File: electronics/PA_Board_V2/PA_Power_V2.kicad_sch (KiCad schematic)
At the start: 35 parts, among them J5 Conn_01x02, Q1 AOD4185, U4 LMR51420, U5 MCP4725, U6 AP2204K-ADJ, U7 TLV70233, U8 INA219AxD

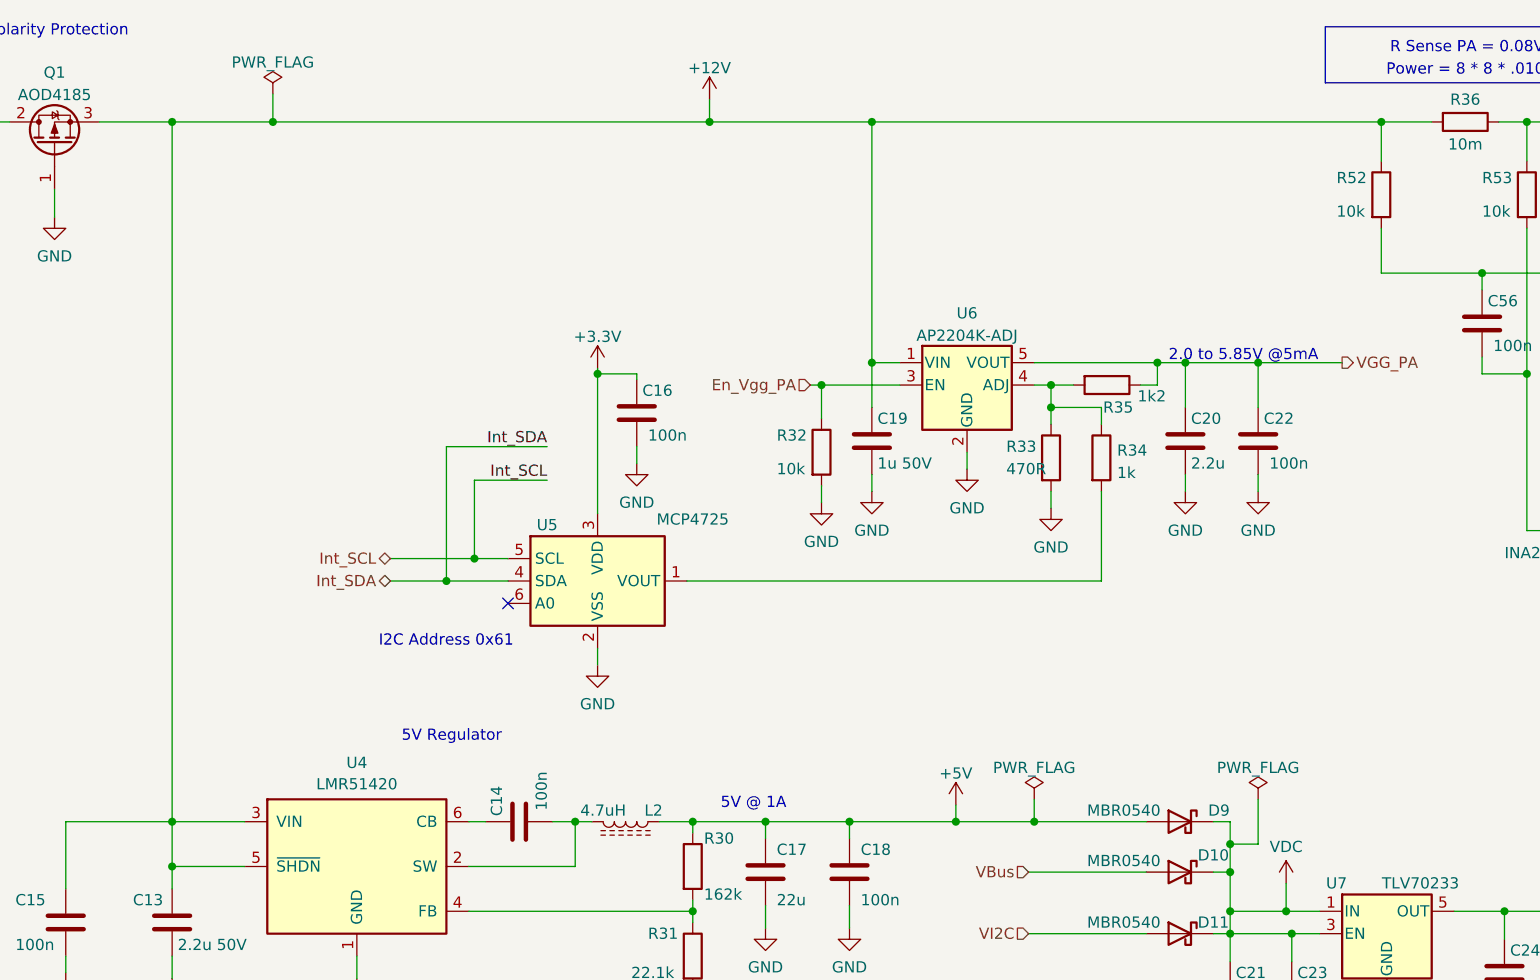
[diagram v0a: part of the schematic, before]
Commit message: Add RF Screen and some PCB and BOM changes
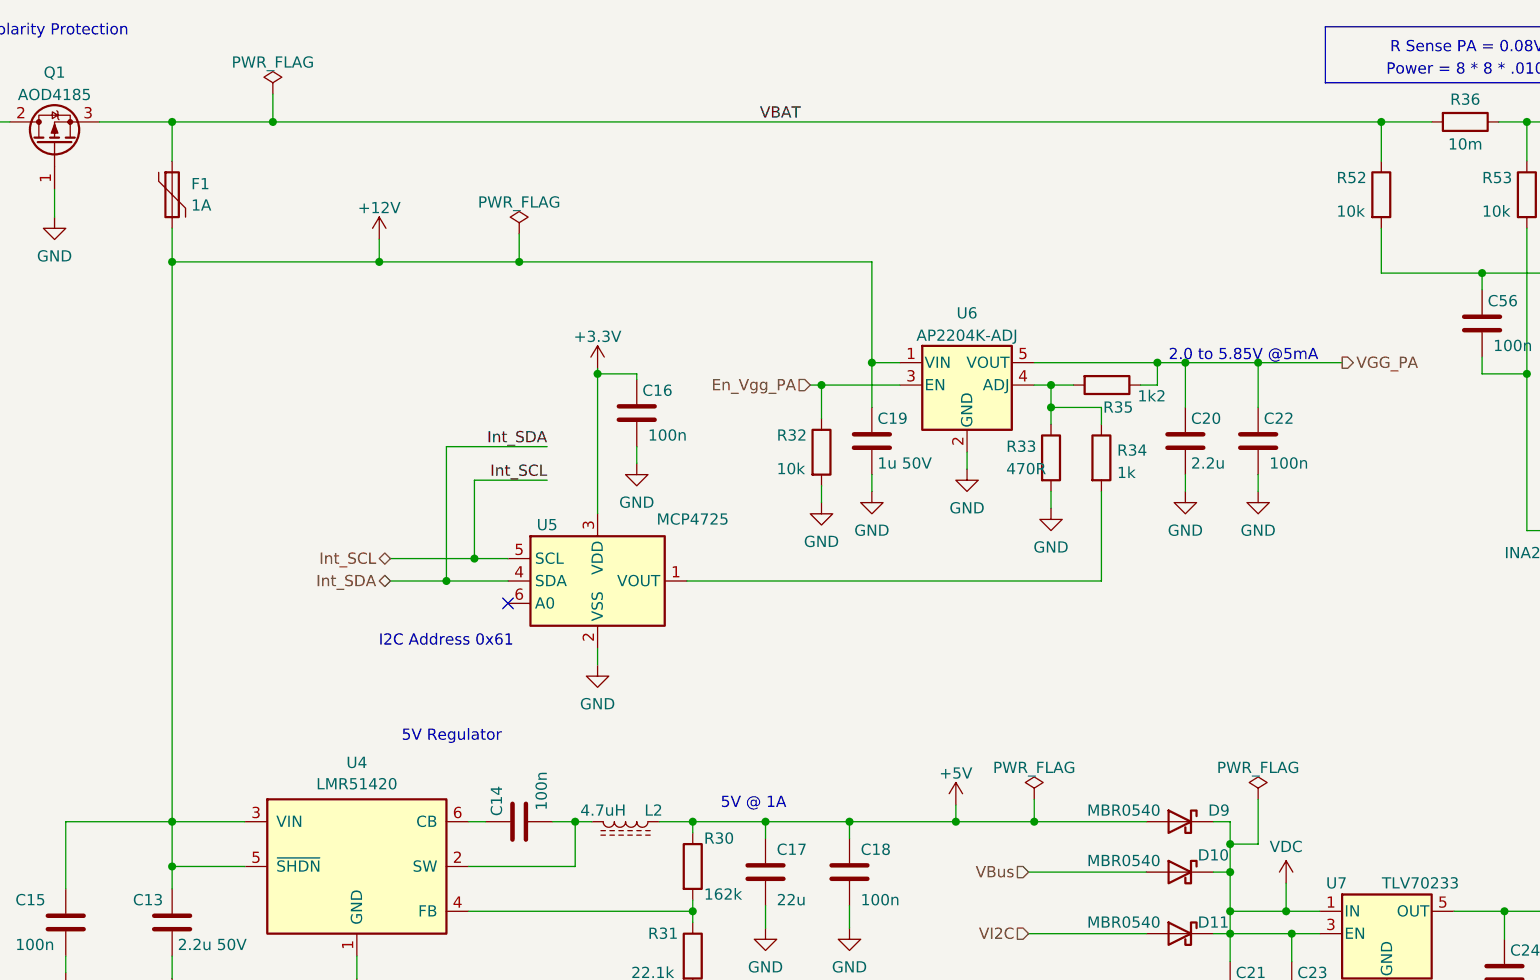
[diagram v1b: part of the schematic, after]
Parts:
- added F1: 1A, Fuse:Fuse_1206_3216Metric, symbol Device:Polyfuse
- J5: Comment (none) -> not fitted; now left out of the parts list
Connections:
- net +12V: now also F1.2; no longer Q1.3 (S), R36.2, R52.1
- new net VBAT: F1.1, Q1.3 (S), R36.2, R52.1

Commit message: Latest version
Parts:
- renumbered C56 to C17, C20 to C22, C13 to C23, C16 to C25, C19 to C26, C15 to C27, C22 to C28, C18 to C29, C26 to C30, C17 to C31, C23 to C38, C21 to C41, C14 to C42, C25 to C46, C24 to C49, D11 to D4, D9 to D7, D10 to D9, J5 to J4, L2 to L5, R35 to R12, R33 to R13, R34 to R14, R32 to R15, R31 to R17, R30 to R20, R53 to R7, R52 to R8, R36 to R9, U8 to U10, U7 to U11, U4 to U6, U5 to U7, U6 to U9
